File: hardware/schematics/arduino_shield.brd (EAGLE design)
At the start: 68.6 x 53.3 mm, 41 parts, among them IC1 LM358KIT, IC2 MAX548, Q1 IRL520N-H, Q2 IRL520N-H, Q3 IRF9Z24, Q4 IRL520N-H, Q5 IRL520N-H, Q6 IRF9Z24, X5 Channel A, X6 Channel B

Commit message: update
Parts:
- removed X5: Channel A, adafruit:STX3100
- removed X6: Channel B, adafruit:STX3100
- added CHANNELA, CHANNELB: (no value), SparkFun-Connectors:STEREOJACK2.5MM_STEREOJACK2.5MM
- moved JP2 60.3 mm to (64.8, 11.4), turned to 90 degrees
- moved R15 49.6 mm to (41.9, 47.0), turned to 0 degrees
- moved JP1 39.9 mm to (62.2, 7.62), turned to 180 degrees
- moved R1 33.9 mm to (26.7, 38.1), turned to 0 degrees
- moved R9 33.2 mm to (22.9, 7.62)
- moved R3 30.6 mm to (34.3, 12.7), turned to 180 degrees
- moved R17 30.2 mm to (21.6, 16.5), turned to 270 degrees
- moved R2 29.6 mm to (34.3, 35.6), turned to 0 degrees
- moved R24 27.4 mm to (34.3, 30.5), turned to 0 degrees
- moved R19 26.7 mm to (27.9, 19.1)
- moved R4 25.3 mm to (27.9, 12.7), turned to 0 degrees
- moved R13 19.8 mm to (14.0, 20.3), turned to 90 degrees
- moved R5 17.3 mm to (34.3, 24.1), turned to 0 degrees
- moved R16 14.5 mm to (22.9, 19.1), turned to 0 degrees
- moved R7 11.7 mm to (6.35, 16.5), turned to 0 degrees
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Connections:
- net N$1: now also CHANNELA.RING1, TR1.6; no longer TR1.4, X5.1
- net N$2: now also CHANNELB.RING1, TR2.6; no longer TR1.6, X5.2, X5.5
- net N$3: now also CHANNELB.SHIELD, CHANNELB.TIP, TR2.4; no longer TR2.6, X6.2, X6.5
- net N$4: now also CHANNELA.SHIELD, CHANNELA.TIP, TR1.4; no longer TR2.4, X6.1
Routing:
- net GND: track 159.9 -> 0.00 mm, vias 2 -> 0
- net +12V: track 130.3 -> 0.00 mm, vias 5 -> 0
- net +5V: track 116.9 -> 0.00 mm, vias 1 -> 0
- net PIN4: track 100.1 -> 0.00 mm, vias 1 -> 0
- net PIN3: track 96.3 -> 0.00 mm, vias 4 -> 0
- net PIN9: track 90.7 -> 0.00 mm, vias 3 -> 0
- net ADC1: track 88.5 -> 0.00 mm
- net N$21: track 74.5 -> 0.00 mm, vias 1 -> 0
- net N$27: track 73.7 -> 0.00 mm, vias 1 -> 0
- net N$41: track 65.1 -> 0.00 mm, vias 2 -> 0
- net PIN5: track 61.1 -> 0.00 mm
- net N$22: track 47.9 -> 0.00 mm
- net PIN11: track 38.9 -> 0.00 mm
- net N$19: track 38.0 -> 0.00 mm, vias 3 -> 0
- net N$40: track 35.8 -> 0.00 mm, vias 2 -> 0
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
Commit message: schematics
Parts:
- removed C4: 100nF, capacitor-wima:C2.5-2
- removed JP1: (no value), jumper:JP2
- removed JP2: M023.5MM, SparkFun-Connectors:SCREWTERMINAL-3.5MM-2
- added C2: 100nF, capacitor-wima:C2.5-2
- Q2, Q5: value IRL520N-H -> IRF9Z24
- Q3, Q6: value IRF9Z24 -> IRL520N-H
- moved C1 46.2 mm to (20.3, 3.81), turned to 270 degrees
- moved R3 36.6 mm to (47.0, 47.0)
- moved R19 28.7 mm to (7.62, 39.4), turned to 180 degrees
- moved R16 22.7 mm to (12.7, 39.4)
- moved Q4 13.3 mm to (34.3, 40.6), turned to 180 degrees
- moved Q5 12.0 mm to (47.0, 40.6), turned to 180 degrees
- moved R17 11.7 mm to (10.2, 14.0), turned to 0 degrees
- moved CHANNELA 11.4 mm to (64.8, 12.7)
- moved Q2 11.4 mm to (41.9, 21.6)
- moved Q3 11.4 mm to (41.9, 10.2)
- moved R12 10.9 mm to (3.81, 14.0), turned to 0 degrees
- moved R4 10.9 mm to (17.8, 8.89)
- moved R18 9.92 mm to (12.7, 45.7)
- moved R1 8.98 mm to (17.8, 39.4)
- moved R20 8.03 mm to (10.2, 8.89), turned to 0 degrees
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- renumbered U$3 to GND
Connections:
- removed net N$7: GND.VIN, JP1.3
- removed net N$8: JP1.1, JP2.1
- net +12V: now also C2.2, GND.VIN, Q2.3, Q5.3; no longer C4.2, JP1.2, Q3.3, Q6.3
- net ADC1: now also Q3.3, Q6.3; no longer Q2.3, Q5.3
- net GND: no longer JP2.2
- net N$19: now also Q3.1; no longer Q2.1
- net N$21: now also Q2.1; no longer Q3.1
- net N$25: now also Q6.1; no longer Q5.1
- net N$27: now also C2.1, Q5.1; no longer C4.1, Q6.1
- net N$35: now also Q2.2; no longer Q3.2
- net N$37: now also Q5.2; no longer Q6.2
- net N$38: now also Q6.2; no longer Q5.2
- net N$39: now also Q3.2; no longer Q2.2
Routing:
- net GND: track 0.00 -> 182.6 mm, vias 0 -> 1
- net +12V: track 0.00 -> 145.4 mm
- net ADC1: track 0.00 -> 129.1 mm
- net N$27: track 0.00 -> 82.0 mm, vias 0 -> 1
- net N$41: track 0.00 -> 75.4 mm, vias 0 -> 1
- net +5V: track 0.00 -> 75.4 mm
- net PIN3: track 0.00 -> 66.6 mm
- net PIN6: track 0.00 -> 63.8 mm, vias 0 -> 2
- net PIN4: track 0.00 -> 61.9 mm
- net PIN9: track 0.00 -> 61.7 mm, vias 0 -> 3
- net N$28: track 0.00 -> 59.8 mm, vias 0 -> 1
- net N$24: track 0.00 -> 51.6 mm, vias 0 -> 1
- net N$19: track 0.00 -> 44.0 mm
- net N$26: track 0.00 -> 41.6 mm, vias 0 -> 1
- net PIN11: track 0.00 -> 40.1 mm
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
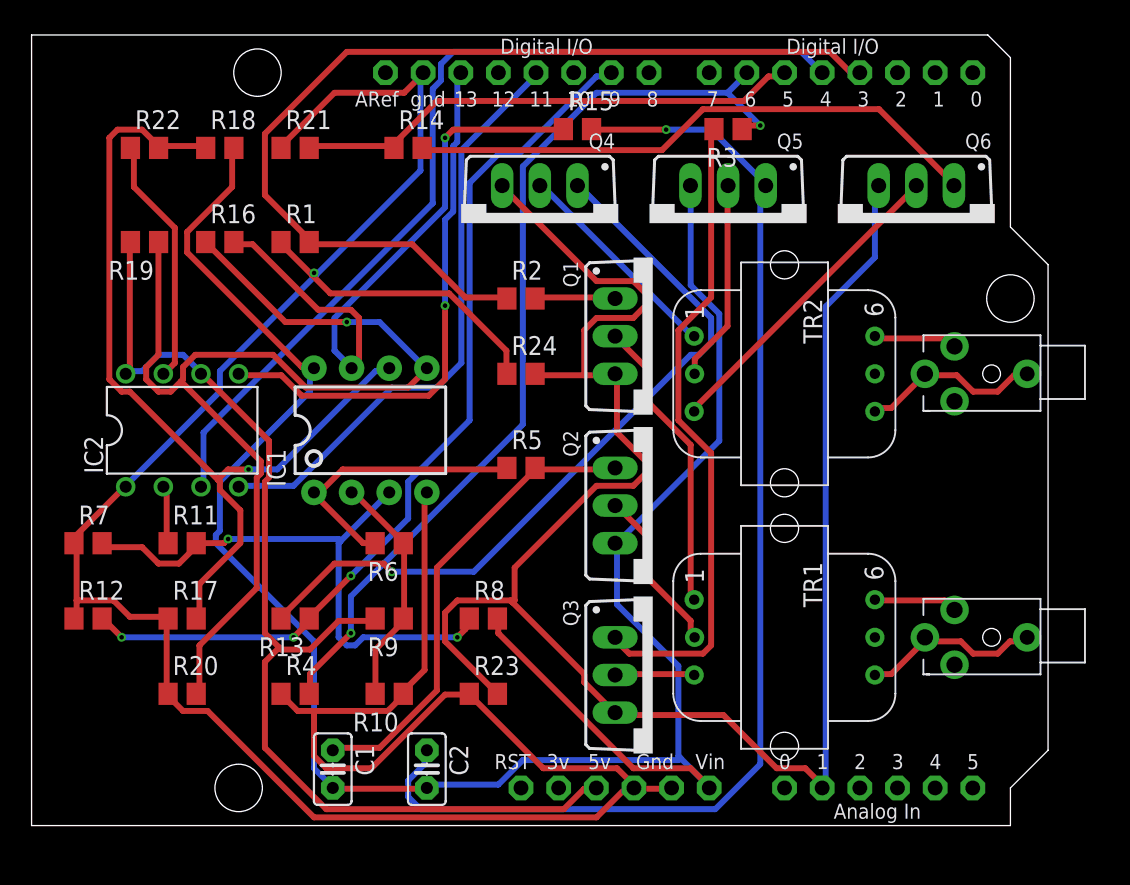
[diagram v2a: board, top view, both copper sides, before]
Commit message: Changes by FluffyBit
done:

- changed grid to 0.1mm to help place components
- forced all components onto 0.1mm grid
- added gnd plane on bottom of board
- added two caps for decoupling the DAC+OP-AMP
- added 10K pull-up on the nCS line to the DAC

ideas:
- add LED on unused digital pin.

fixes
- IC1G2 swaped +/- input to make negative feedback

notes:

no decoupling on +5V (fixed)

no bulk decoupling on +12V or +5V
-> suggest 10uF 0805 on 5V near DAC
-> suggest 10uF near op-amp area
-> suggest 47uF or 100uF near the +12V transformer drive

bias for op-amps seem to be either 5V or 12V (not consistent)

if digital-io is not important then you could:
- 5->8
- 3->7

todo:
- check body-diode on pfets driving transformer centre-tap
 -> think it is ok, diode goes drain-to-source on selected FET
 -> source is the outer pin (drain middle)
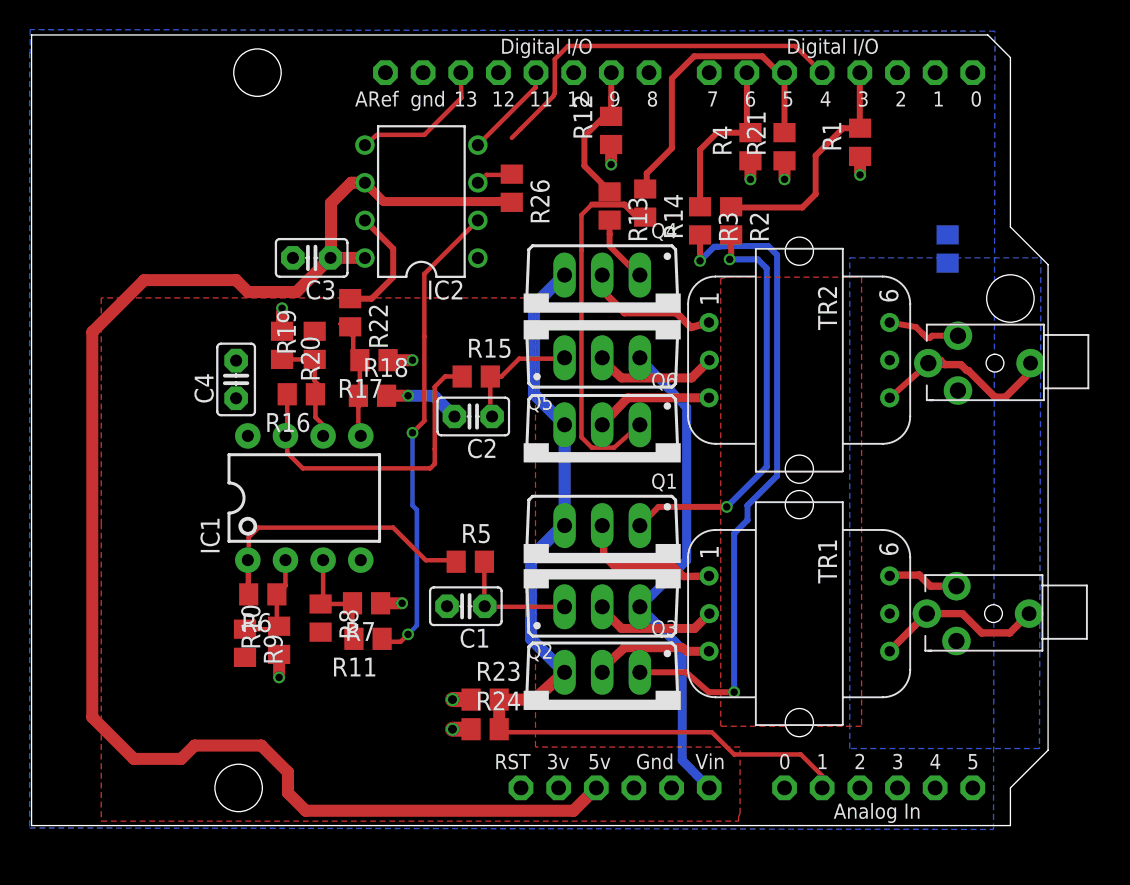
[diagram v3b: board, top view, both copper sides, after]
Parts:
- added C3, C4: 100nF, capacitor-wima:C2.5-2
- added R25: 0R, eagle-ltspice:R0805
- added R26: 10k, eagle-ltspice:R0805
- moved R12 48.3 mm to (39.1, 46.9), turned to 90 degrees
- moved R4 48.0 mm to (48.5, 45.8), turned to 90 degrees
- moved R1 38.7 mm to (55.9, 46.1), turned to 90 degrees
- moved R13 35.0 mm to (39.0, 41.8), turned to 270 degrees
- moved R21 33.0 mm to (50.8, 45.8), turned to 90 degrees
- moved Q6 26.6 mm to (38.5, 24.5)
- moved R20 24.5 mm to (16.9, 32.4), turned to 270 degrees
- moved R24 24.1 mm to (30.6, 6.50)
- moved C2 24.0 mm to (29.8, 27.6), turned to 180 degrees
- moved IC2 22.3 mm to (26.3, 42.1), turned to 90 degrees
- moved R17 21.7 mm to (23.1, 31.4), turned to 180 degrees
- moved R18 19.6 mm to (23.0, 29.0)
- moved R7 19.2 mm to (22.6, 15.0), turned to 180 degrees
- moved R15 18.0 mm to (30.0, 30.3)
- moved R22 17.8 mm to (21.5, 34.6), turned to 270 degrees
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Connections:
- new net SHIELD: R25.2
- net +12V: now also C4.1
- net +5V: now also C3.1, R26.2
- net GND: now also C3.2, C4.2, R25.1
- net N$28: now also IC1.5; no longer IC1.6
- net N$41: now also IC1.6; no longer IC1.5
- net PIN4: now also R26.1
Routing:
- net GND: track 182.6 -> 13.8 mm, vias 1 -> 10
- net +12V: track 145.4 -> 38.7 mm, vias 0 -> 1
- net N$27: track 82.0 -> 8.26 mm, vias 1 -> 0
- net ADC1: track 129.1 -> 61.5 mm
- net N$41: track 75.4 -> 7.91 mm, vias 1 -> 0
- net PIN9: track 61.7 -> 9.77 mm, vias 3 -> 0
- net PIN6: track 63.8 -> 11.9 mm, vias 2 -> 0
- net PIN3: track 66.6 -> 16.2 mm
- net N$28: track 59.8 -> 9.59 mm, vias 1 -> 0
- net N$24: track 51.6 -> 4.60 mm, vias 1 -> 0
- net PIN4: track 61.9 -> 27.9 mm
- net PIN11: track 40.1 -> 6.50 mm
- net N$22: track 38.8 -> 7.64 mm, vias 2 -> 0
- net N$5: track 3.99 -> 32.4 mm, vias 0 -> 2
- net +5V: track 75.4 -> 103.4 mm
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- added copper zone on layer 1, net +12V
- added copper zone on layer 16, net GND
- added copper zone on layer 16, net SHIELD
- added copper zone on layer 1, net SHIELD2

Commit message: A Lot of work done :D
Assuming the Transformer is correct, we have a version we can send to a fab house
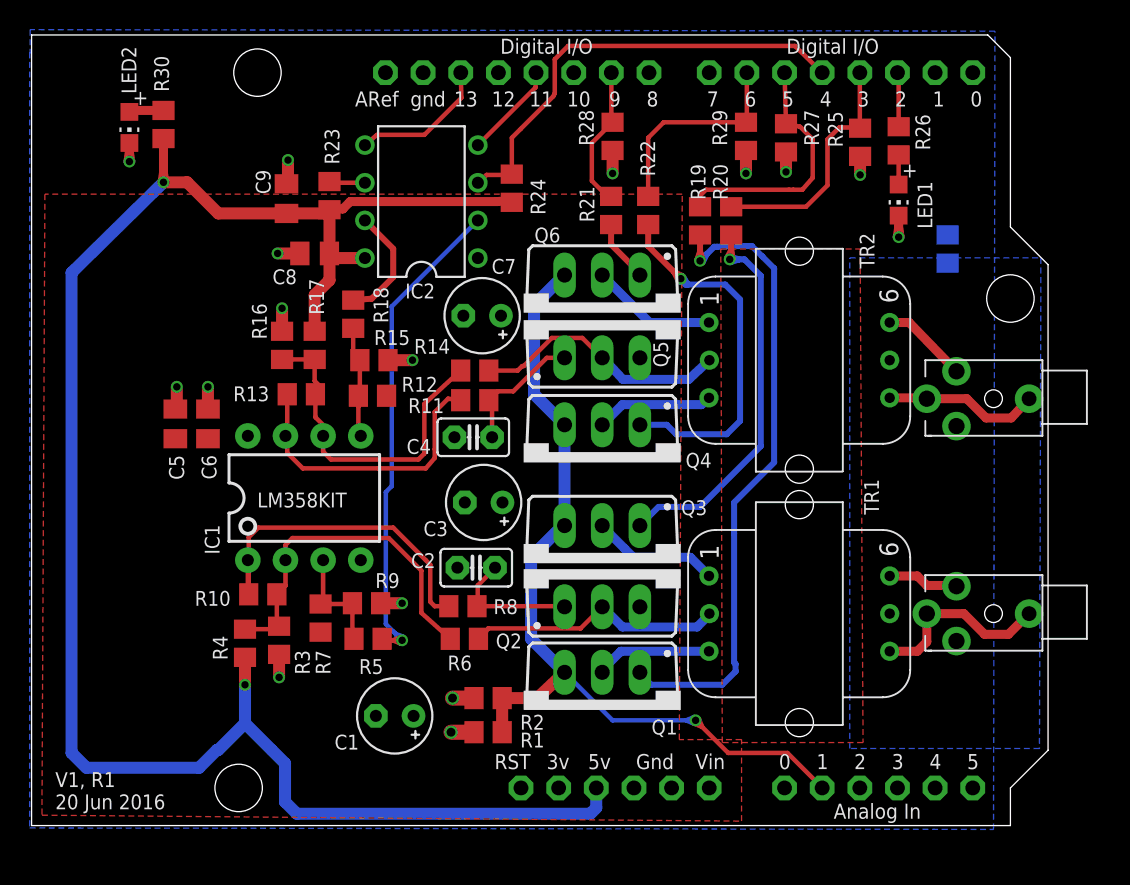
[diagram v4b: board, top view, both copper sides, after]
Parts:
- added C5, C9: 10uF, rcl:C0805K
- added C6, C8: 100nF, rcl:C0805K
- added C7: 47uF, rcl:E2,5-5
- added LED1, LED2: (no value), adafruit:CHIP-LED0805
- added R100: 0R, eagle-ltspice:R0805
- added R27, R28, R29: 100k, eagle-ltspice:R0805
- added R30: 560R, rcl:R0805
- C1, C3: value 100nF -> 47uF; device capacitor-wima:C2.5-2 -> rcl:E2,5-5
- R1: value 100k -> 1R
- R10: value 200k -> 100k
- R11, R19, R21, R22, R8: value 100k -> 10k
- R13, R15, R3, R5: value 10k -> 100k
- R14: value 10k -> xk
- R16, R4: value 100k -> 200k
- R2: value 10k -> 1R
- R20: value 200k -> 10k
- R23, R24: value 1R -> 10k
- R25: value 0R -> 100k
- R26: value 10k -> 560R; device eagle-ltspice:R0805 -> rcl:R0805
- R6: value 100k -> xk
- moved R1 47.1 mm to (30.8, 6.30), turned to 0 degrees
- moved R4 46.0 mm to (16.7, 12.5)
- moved R3 41.9 mm to (14.4, 12.3)
- moved R24 36.5 mm to (32.4, 43.0), turned to 270 degrees
- moved R2 36.1 mm to (30.8, 8.60), turned to 0 degrees
- moved R23 35.6 mm to (20.1, 42.5), turned to 270 degrees
- moved R20 31.4 mm to (47.2, 40.8)
- moved R19 27.3 mm to (45.1, 40.8), turned to 270 degrees
- moved R26 26.3 mm to (58.5, 46.2), turned to 90 degrees
- moved R13 24.4 mm to (18.2, 29.1), turned to 180 degrees
- moved R12 24.1 mm to (23.0, 29.0), turned to 0 degrees
- moved R22 21.3 mm to (41.6, 41.5)
- moved C3 20.2 mm to (30.5, 21.8)
- moved R11 17.6 mm to (29.9, 28.7), turned to 0 degrees
- moved C4 16.5 mm to (29.8, 26.2), turned to 180 degrees
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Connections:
- new net N$7: IC2.6, R23.1
- new net N$8: LED1.A, R26.1
- new net N$9: LED2.A, R30.1
- net +12V: now also C1.+, C3.+, C4.2, C5.1, C6.1, C7.+, R12.2, R7.2; no longer C1.2, C4.1, R18.2, R8.2
- net +5V: now also C8.1, C9.1, R17.2, R23.2, R24.2, R3.2, R30.2; no longer C3.1, IC2.6, R19.2, R26.2, R9.2
- net ADC1: now also R1.2, R2.2; no longer R23.2, R24.2
- net GND: now also C1.-, C3.-, C5.2, C6.2, C7.-, C8.2, C9.2, LED1.C, LED2.C, R100.1, R15.1, R16.1, R2.1, R27.1, R28.1, R29.1, R9.1; no longer C3.2, C4.2, R10.1, R12.1, R17.1, R20.1, R21.1, R23.1, R24.1, R7.1
- net N$18: now also Q3.1, R20.2; no longer Q1.1, R2.2
- net N$19: now also Q1.1, R19.2; no longer Q3.1, R3.2
- net N$20: now also R10.2, R8.1; no longer R5.1, R6.2
- net N$21: now also C2.1, R8.2; no longer C1.1, R5.2
- net N$22: now also R5.2, R7.1, R9.2; no longer R11.2, R7.2, R8.1
- net N$24: now also Q6.1, R21.2; no longer Q4.1, R13.2
- net N$25: now also Q4.1, R22.2; no longer Q6.1, R14.2
- net N$26: now also R11.1, R13.2; no longer R15.1, R16.2
- net N$27: now also C4.1, R11.2; no longer C2.1, R15.2
- net N$28: now also R12.1, R15.2, R18.2; no longer R17.2, R18.1, R22.2
- net N$34: now also Q3.2; no longer Q1.2
- net N$35: now also R6.2
- net N$36: now also Q6.2; no longer Q4.2
- net N$37: now also R14.2
- net N$38: now also Q4.2; no longer Q6.2
- net N$39: now also Q1.2; no longer Q3.2
- net N$40: now also R10.1, R3.1, R4.2; no longer R10.2, R9.1
- net N$41: now also R13.1, R14.1, R16.2, R17.1; no longer R16.1, R19.1, R20.2
- net N$5: now also R5.1; no longer R11.1
- net N$6: now also R18.1; no longer R22.1
- net PIN2: now also R26.2
- net PIN3: now also R20.1, R25.2; no longer R1.2, R2.1
- net PIN4: now also R24.1; no longer R26.1
- net PIN5: now also R19.1, R27.2; no longer R14.1, R21.2
- net PIN6: now also R22.1, R29.2; no longer R3.1, R4.2
- net PIN9: now also R21.1, R28.2; no longer R12.2, R13.1
- net SHIELD: now also R100.2; no longer R25.2
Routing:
- net +12V: track 38.7 -> 0.00 mm, vias 1 -> 0
- net +5V: track 103.4 -> 128.4 mm, vias 0 -> 2
- net N$40: track 7.14 -> 23.9 mm
- net N$41: track 7.91 -> 22.9 mm
- net GND: track 13.8 -> 26.7 mm, vias 10 -> 16
- net N$35: track 8.34 -> 18.2 mm
- net N$37: track 8.58 -> 17.5 mm
- net PIN5: track 21.0 -> 17.1 mm
- net N$5: track 32.4 -> 36.2 mm, vias 2 -> 1
- net PIN2: track 0.00 -> 3.68 mm
- net N$25: track 24.8 -> 28.0 mm, vias 0 -> 1
- net PIN4: track 27.9 -> 30.6 mm
- net PIN6: track 11.9 -> 14.4 mm
- net N$7: track 0.00 -> 2.40 mm
- net N$9: track 0.00 -> 2.34 mm
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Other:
- board text added: "V1, R1 20 Jun 2016"
